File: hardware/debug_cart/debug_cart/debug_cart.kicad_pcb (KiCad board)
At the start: 2 copper layers, 48 x 66.1 mm, 38 parts, among them CON1 vectrex-edge-connector, J1 USB_C_Receptacle_USB2.0, Q1 BSS138, Q2 BSS138, Q3 BSS138, U1 RP2040, U2 SN74LVC245APW, U3 SN74LVC245APW, U4 SN74LVC245APW, U5 AMS1117-3.3, U6 APS6404L-3SQRx-SN, U7 W25Q16JVSS, Y1 Crystal_GND24

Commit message: hw(debug_cart): rewire U2/U3 DIR to ABUS_DIR for bus mastering
Single GPIO controls U2/U3 buffer direction (LOW=Vectrex→MCU ROM mode,
HIGH=MCU→Vectrex bus master mode). /OE of U2/U3 stays at GND.

- Remove R7/R8 (CART_RW divider): R/W sensing dropped (cart is read-only)
- New net ABUS_DIR connects U2.1, U3.1 and MCU pin GP24
- CART_RW now only present at CON1 card edge (NC on MCU side)

PCB netlist synced (3× ABUS_DIR labels in .pcb); physical routing pending.

Note: this checkpoint is taken BEFORE migrating U1 from RP2040 (QFN-56)
to RP2350A (QFN-60) — current .sch/.pcb still target RP2040 even though
firmware uses rp235x-hal.

Co-Authored-By: Claude Opus 4.7 <noreply@anthropic.com>
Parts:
- added H3: MountingHole, vextreme:Mounting_Hole_D3.7mm, F.Cu at (181.3, 56.7)
- renumbered R7 to R10, R8 to R11, R9 to R12, R1 to R4, R2 to R5, R3 to R6, R6 to R9
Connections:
- U1 pad 36: GP24_RW -> ABUS_DIR
- U2 pad 1: GND -> ABUS_DIR
- U3 pad 1: GND -> ABUS_DIR

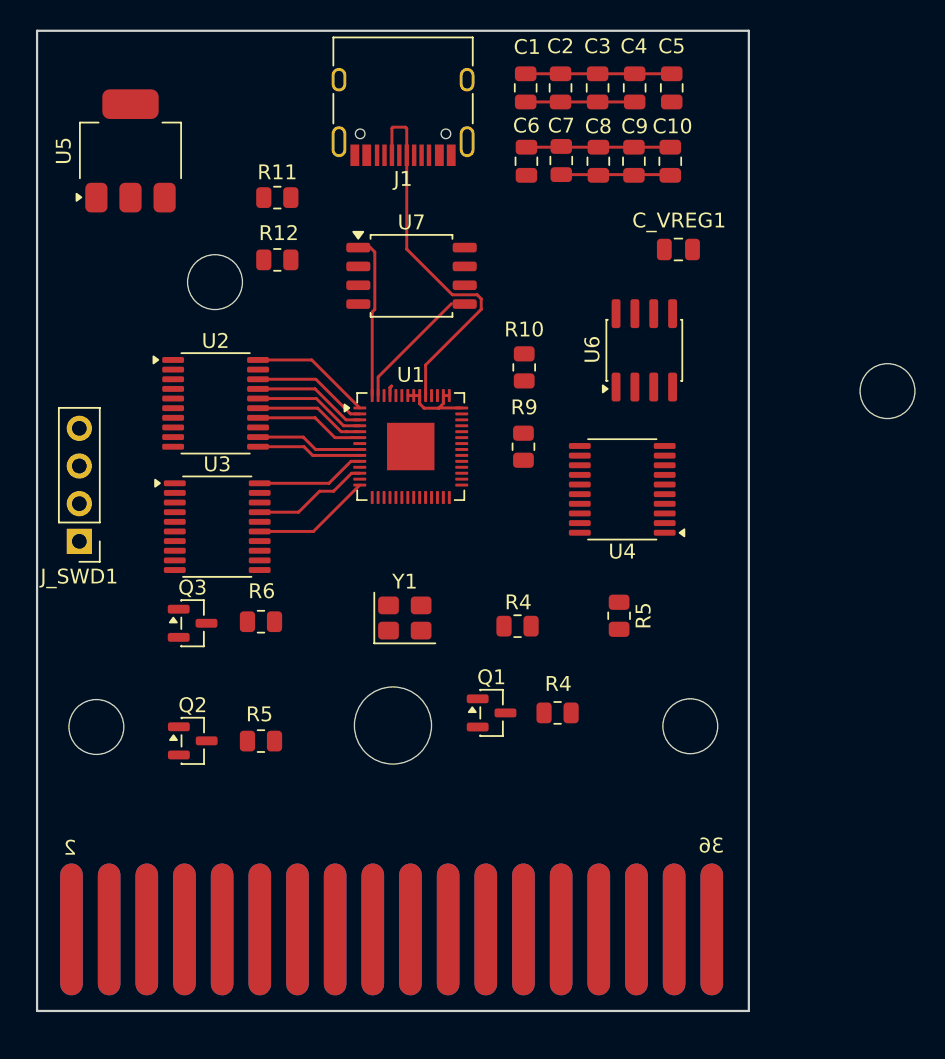
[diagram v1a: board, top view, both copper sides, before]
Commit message: hw(debug_cart): full PCB layout — 4 layers, all components placed and routed
PCB stackup upgraded to 4 layers for cleaner routing of the Vectrex bus,
QSPI memory bus, and USB differential pair:
  - F.Cu (top signal + components)
  - In1.Cu (GND plane)
  - In2.Cu (+3V3 plane)
  - B.Cu (bottom signal + decoupling)

Final BOM (all references):
  ICs:       U1 RP2350B, U2/U3/U4 74LVC245A buffers, U5 AMS1117 LDO,
             U6 APS6404L PSRAM, U7 W25Q64JV flash, U8 74LVC1G07 1-gate
  Transistors: Q1-Q4 BSS138 (HALT/NMI/RST/IRQ open-drain)
  Resistors: R1-R15 (4× BSS138 pullups, /OE divider, CART_RW pullup,
             USB-C CC pulldowns, RUN pullup, SD_CS pullup, PB6/CART
             dividers, IRQ pullup)
  Caps:      C1-C24 (MCU decoupling per rail, U6/U7 decoupling,
             3× decoupling for new RP2350B rails, SD bulk, LDO bulks,
             crystal load caps)
  Connectors: CON1 card edge (DNP for BOM), J1 USB-C, J2 microSD,
             J_UART1 1×4 header, J_SWD1 SWD header
  Other:     SW1 BOOTSEL button, Y1 12MHz crystal + load caps,
             TP_BOOTSEL + TP_RESET test points

Schematic ERC: 0 errors, 0 warnings (2 LDO bypass mode exclusions noted)
PCB DRC:       0 errors, 0 warnings

All components match COMPONENTS.md / pins.rs / MIGRATION_*.md docs.

The cart edge uses ENIG gold finger plating with 45° bevel (specified at
fabrication time, not in the design). PCB ready for Gerber generation.

Co-Authored-By: Claude Opus 4.7 <noreply@anthropic.com>
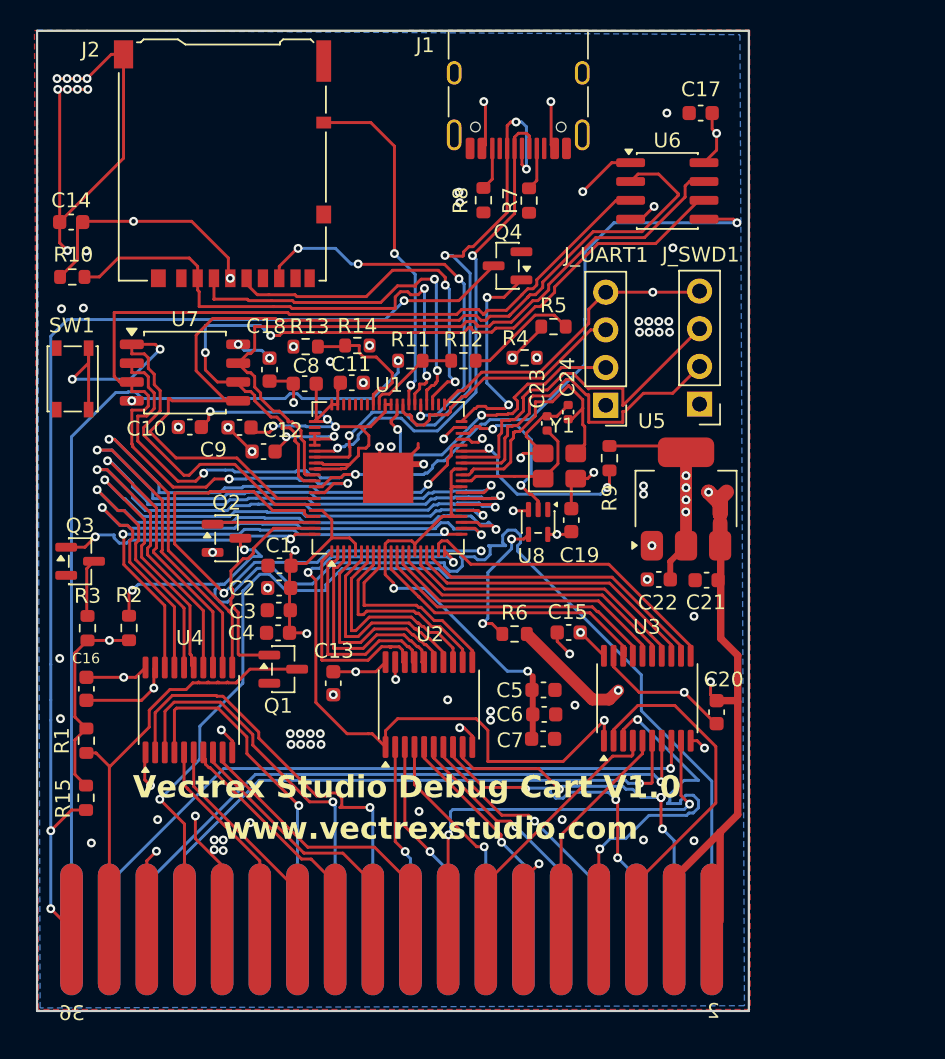
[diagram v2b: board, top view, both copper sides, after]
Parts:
- removed C_VREG1: 1 µF, Capacitor_SMD:C_0805_2012Metric
- removed H1, H2, H3, H4: MountingHole, vextreme:Mounting_Hole_D3.7mm
- removed H5: MountingHole, vextreme:Mounting_Hole_D5.2mm
- removed the R4 at (156.4, 72.5)
- removed the R4 at (159.1, 78.4)
- removed the R5 at (163.2, 71.8)
- removed the R5 at (139.1, 80.3)
- added C11: 100nf, Capacitor_SMD:C_0603_1608Metric, F.Cu at (145.2, 56.1)
- added C12: 1uf, Capacitor_SMD:C_0603_1608Metric, F.Cu at (139.3, 60.8)
- added C13: 100nf, Capacitor_SMD:C_0603_1608Metric, F.Cu at (144.0, 76.4)
- added C14: 10uf, Capacitor_SMD:C_0603_1608Metric, F.Cu at (126.3, 45.3)
- added C15: 100nf, Capacitor_SMD:C_0603_1608Metric, F.Cu at (159.8, 73.0)
- added C16: 100nf, Capacitor_SMD:C_0603_1608Metric, F.Cu at (127.3, 76.8)
- added C17: 100nf, Capacitor_SMD:C_0603_1608Metric, F.Cu at (168.8, 38.0)
- added C18: 100nf, Capacitor_SMD:C_0603_1608Metric, F.Cu at (139.7, 55.2)
- added C19: 100nf, Capacitor_SMD:C_0603_1608Metric, F.Cu at (160.0, 65.4)
- added C20: 100nf, Capacitor_SMD:C_0603_1608Metric, F.Cu at (169.8, 78.3)
- added C21: 10nf, Capacitor_SMD:C_0603_1608Metric, F.Cu at (169.2, 69.5)
- added C22: 10nf, Capacitor_SMD:C_0603_1608Metric, F.Cu at (165.9, 69.4)
- added C23: 22pf, Capacitor_SMD:C_0402_1005Metric, F.Cu at (158.4, 58.9)
- added C24: 22pf, Capacitor_SMD:C_0402_1005Metric, F.Cu at (159.8, 58.1)
- added J2: Micro_SD_Card_Det_Hirose_DM3AT, Connector_Card:microSD_HC_Hirose_DM3AT-SF-PEJM5, F.Cu at (136.5, 41.4)
- added J_UART1: Conn_01x04, Connector_PinHeader_2.54mm:PinHeader_1x04_P2.54mm_Vertical, F.Cu at (162.3, 57.6)
- added Q4: BSS138, Package_TO_SOT_SMD:SOT-23, F.Cu at (155.7, 48.2)
- added R1: 10K, Resistor_SMD:R_0603_1608Metric, F.Cu at (127.3, 80.3)
- added R13: 10K, Resistor_SMD:R_0603_1608Metric, F.Cu at (142.1, 53.7)
- added R14: 18K, Resistor_SMD:R_0603_1608Metric, F.Cu at (145.6, 53.6)
- added R15: 10K, Resistor_SMD:R_0603_1608Metric, F.Cu at (127.3, 84.1)
- added R2: 10K, Resistor_SMD:R_0603_1608Metric, F.Cu at (130.2, 72.7)
- added R3: 10K, Resistor_SMD:R_0603_1608Metric, F.Cu at (127.4, 72.7)
- added R4: 10K, Resistor_SMD:R_0603_1608Metric, F.Cu at (156.9, 54.5)
- added R5: 18K, Resistor_SMD:R_0603_1608Metric, F.Cu at (158.8, 52.4)
- added R7: 5K1, Resistor_SMD:R_0603_1608Metric, F.Cu at (157.2, 43.9)
- added R8: 5K1, Resistor_SMD:R_0603_1608Metric, F.Cu at (154.1, 43.8)
- added SW1: SW_Push, Button_Switch_SMD:SW_SPST_PTS810, F.Cu at (126.4, 55.9)
- added U8: 74LVC1G07, Package_TO_SOT_SMD:SOT-353_SC-70-5, F.Cu at (157.8, 65.5)
- C1, C10, C2, C3, C4, C5, C6, C7, C8, C9: footprint Capacitor_SMD:C_0805_2012Metric -> Capacitor_SMD:C_0603_1608Metric
- R10: value 18K -> 10k; footprint Resistor_SMD:R_0805_2012Metric -> Resistor_SMD:R_0603_1608Metric
- R11: value 5K1 -> 10K; footprint Resistor_SMD:R_0805_2012Metric -> Resistor_SMD:R_0603_1608Metric
- R12: value 5K1 -> 18K; footprint Resistor_SMD:R_0805_2012Metric -> Resistor_SMD:R_0603_1608Metric
- R6: value 10K -> 10k; footprint Resistor_SMD:R_0805_2012Metric -> Resistor_SMD:R_0603_1608Metric
- R9: value 10K -> 100K; footprint Resistor_SMD:R_0805_2012Metric -> Resistor_SMD:R_0603_1608Metric
- U1: value RP2040 -> RP2350B; footprint Package_DFN_QFN:QFN-56-1EP_7x7mm_P0.4mm_EP3.2x3.2mm -> Package_DFN_QFN:QFN-80-1EP_10x10mm_P0.4mm_EP3.4x3.4mm
- U6: value APS6404L-3SQRx-SN -> APS6404L-3SQR-SN
- moved U5 44.2 mm to (167.8, 64.0)
- moved C4 43.9 mm to (140.2, 73.0), turned to 180 degrees
- moved J_SWD1 42.8 mm to (168.7, 57.6)
- moved C5 41.5 mm to (158.2, 76.8), turned to 0 degrees
- moved C3 41.3 mm to (140.3, 71.5), turned to 180 degrees
- moved C7 39.0 mm to (158.1, 80.2), turned to 0 degrees
- moved C2 38.7 mm to (140.3, 70.0), turned to 180 degrees
- moved C6 37.3 mm to (158.2, 78.5), turned to 0 degrees
- moved C10 37.0 mm to (134.3, 59.1), turned to 180 degrees
- moved C1 36.2 mm to (140.3, 68.5), turned to 180 degrees
- moved U4 32.8 mm to (134.2, 78.2), turned to 90 degrees
- moved C9 32.1 mm to (137.7, 59.1), turned to 180 degrees
- moved U3 31.2 mm to (165.2, 77.4), turned to 90 degrees
- moved R10 31.1 mm to (126.4, 49.0), turned to 180 degrees
- moved U2 24.9 mm to (150.4, 77.8), turned to 90 degrees
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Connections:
- net GP10 renamed A10
- net GP11 renamed A11
- net GP4 renamed A4
- net GP5 renamed A5
- net GP6 renamed A6
- net GP7 renamed A7
- net GP8 renamed A8
- net GP9 renamed A9
- C5 pad 1: +5V -> +3V3
- C6 pad 1: +5V -> +3V3
- CON1 pad 1: CART_HALT -> CART_nHALT
- CON1 pad 12: CART_OE -> CART_nOE
- CON1 pad 16: CART_CE -> CART_nCE
- CON1 pad 18: CART_7D -> CART_D7
- CON1 pad 2: +3V3 -> +5V
- CON1 pad 34: CART_NMI -> CART_nNMI
- CON1 pad 36: CART_IRQ -> CART_nIRQ
- CON1 pad 4: +3V3 -> +5V
- Q1 pad 1: GP26_nNMI -> nNMI_DRIVE
- Q1 pad 3: nNMI -> CART_nNMI
- Q2 pad 1: GP27_nHALT -> nHALT_DRIVE
- Q2 pad 3: nHALT -> CART_nHALT
- Q3 pad 1: GP28_nRST -> nRST_DRIVE
- R10 pad 1: GP25_nOE -> SD_CS
- R10 pad 2: GND -> +3V3
- R11 pad 1: CC1 -> CART_PB6
- R11 pad 2: GND -> PB6_SENSE
- R12 pad 1: CC2 -> PB6_SENSE
- R6 pad 1: +5V -> CART_RW
- R6 pad 2: TP_RESET -> +5V
- R9 pad 1: CART_nOE -> +3V3
- R9 pad 2: GP25_nOE -> RUN
- U1 pad 1: +3V3 -> A0
- U1 pad 15: GP12 -> +3V3
- U1 pad 16: GP13 -> A12
- U1 pad 17: GP14 -> A13
- U1 pad 18: GP15 -> A14
- U1 pad 19: GND -> nCE
- U1 pad 2: GP0 -> A1
- U1 pad 20: XTAL_IN -> ABUS_DIR
- U1 pad 21: XTAL_OUT -> D0
- U1 pad 22: +3V3 -> D1
- U1 pad 23: +3V3 -> D2
- U1 pad 24: SWD_CLK -> +3V3
- U1 pad 25: SWD_IO -> D3
- U1 pad 26: DIR_CTRL -> D4
- U1 pad 27: GP16 -> D5
- U1 pad 28: GP17 -> D6
- U1 pad 29: GP18 -> +3V3
- U1 pad 3: GP1 -> A2
- U1 pad 30: GP19 -> XTAL_IN
- U1 pad 31: GP20 -> XTAL_OUT
- U1 pad 32: GP21 -> +3V3
- U1 pad 33: +3V3 -> SWD_CLK
- U1 pad 34: GP22 -> SWD_IO
- U1 pad 35: GP23 -> RUN
- U1 pad 36: ABUS_DIR -> D7
- U1 pad 37: GP25_nOE -> DIR_CTRL
- U1 pad 38: GP26_nNMI -> CART_RW_DRIVE
- U1 pad 39: GP27_nHALT -> nOE_SENSE
- U1 pad 4: GP2 -> A3
- U1 pad 40: GP28_nRST -> nIRQ_DRIVE
- U1 pad 41: PSRAM_CS -> +3V3
- U1 pad 42: +3V3 -> unconnected-(U1-GPIO33-Pad42)
- U1 pad 43: +3V3 -> SD_SCK
- U1 pad 44: +3V3 -> SD_MOSI
- U1 pad 45: Net-(U1-VREG_VOUT) -> SD_MISO
- U1 pad 46: USB_DM -> SD_CS
- U1 pad 47: USB_DP -> SD_CD
- U1 pad 48: +3V3 -> UART_TX
- U1 pad 49: +3V3 -> UART_RX
- U1 pad 5: GP3 -> +3V3
- U1 pad 51: QSPI_SD3 -> +3V3
- U1 pad 52: QSPI_SCK -> PB6_SENSE
- U1 pad 53: QSPI_SD0 -> CART_SENSE
- U1 pad 54: QSPI_SD2 -> unconnected-(U1-GPIO43/ADC3-Pad54)
- U1 pad 55: QSPI_SD1 -> unconnected-(U1-GPIO44/ADC4-Pad55)
- U1 pad 56: QSPI_CSn -> unconnected-(U1-GPIO45/ADC5-Pad56)
- U1 pad 57: GND -> unconnected-(U1-GPIO46/ADC6-Pad57)
- U2 pad 15: GP3 -> A3
- U2 pad 16: GP2 -> A2
- U2 pad 17: GP1 -> A1
- U2 pad 18: GP0 -> A0
- U3 pad 11: GP23 -> nCE
- U3 pad 12: GP14 -> A14
- U3 pad 13: GP13 -> A13
- U3 pad 14: GP12 -> A12
- U4 pad 1: GND -> DIR_CTRL
- U4 pad 11: GP22 -> D7
- U4 pad 12: GP21 -> D6
- U4 pad 13: GP20 -> D5
- U4 pad 14: GP19 -> D4
- U4 pad 15: GP18 -> D3
- U4 pad 16: GP17 -> D2
- U4 pad 17: GP16 -> D1
- U4 pad 18: GP15 -> D0
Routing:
- net GND: track 19.6 -> 226.0 mm, vias 0 -> 81
- net +5V: track 0.00 -> 177.1 mm, vias 0 -> 6
- net +3V3: track 36.0 -> 185.3 mm, vias 0 -> 24
- net CART_nIRQ: track 0.00 -> 75.4 mm, vias 0 -> 3
- net CART_nHALT: track 0.00 -> 73.4 mm, vias 0 -> 2
- net QSPI_SD2: track 0.00 -> 69.0 mm, vias 0 -> 2
- net PSRAM_CS: track 0.00 -> 68.8 mm, vias 0 -> 3
- net QSPI_SD0: track 0.84 -> 66.5 mm, vias 0 -> 3
- net QSPI_SD1: track 8.25 -> 68.0 mm
- net CART_PB6: track 0.00 -> 58.5 mm, vias 0 -> 1
- net QSPI_SCK: track 0.00 -> 54.0 mm, vias 0 -> 2
- net CART_RW: track 0.00 -> 53.8 mm, vias 0 -> 3
- net D6: track 0.00 -> 50.0 mm, vias 0 -> 2
- net QSPI_SD3: track 0.00 -> 48.9 mm
- net D5: track 0.00 -> 48.5 mm, vias 0 -> 2
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- added copper zone on In1.Cu, net +3V3
- added copper zone on B.Cu, net GND
- added copper zone on F.Cu, net GND
- added copper zone on In2.Cu, net GND
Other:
- copper layers 2 -> 4
- board text added: "Vectrex Studio Debug Cart V1.0"
- board text added: "www.vectrexstudio.com"
